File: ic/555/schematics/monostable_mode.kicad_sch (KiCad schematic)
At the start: 7 parts, among them U1 7555

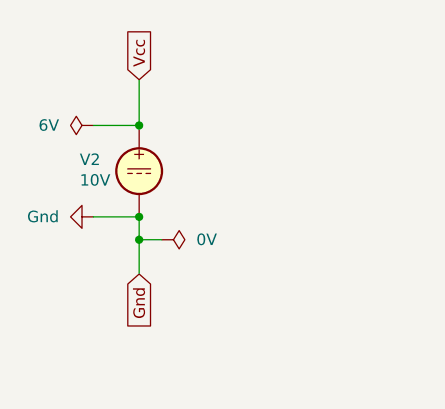
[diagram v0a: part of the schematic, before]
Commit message: feat: add monostable mode 555 timer circuit documentation and schematics
Adds practical example of 555 timer in monostable mode and updates the
README.

Breaking changes: None

Resolves: None
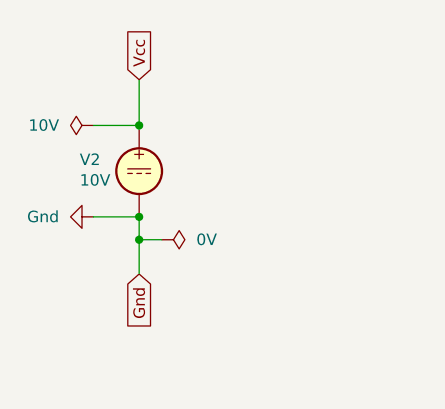
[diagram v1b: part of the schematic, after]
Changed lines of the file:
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@@
 			)
 		)
-		(property "Value" "6V"
+		(property "Value" "10V"
 			(at 21.59 26.6699 90)
 			(effects

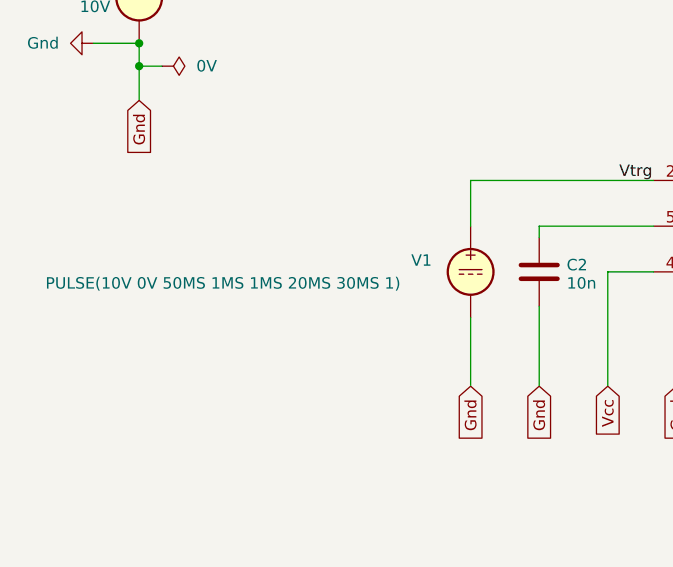
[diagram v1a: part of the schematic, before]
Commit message: feat: add LM741 op-amp with differential amplifier example
Adds the LM741 operational amplifier to the repository, including a
detailed schematic of an non inverting differential amplifier circuit.
The schematic is provided in KiCad format along with an SVG
version for easy viewing. Additionally, oscilloscope screenshots
demonstrate the amplifier's performance under various input conditions.

Breaking changes: None

Resolves: None
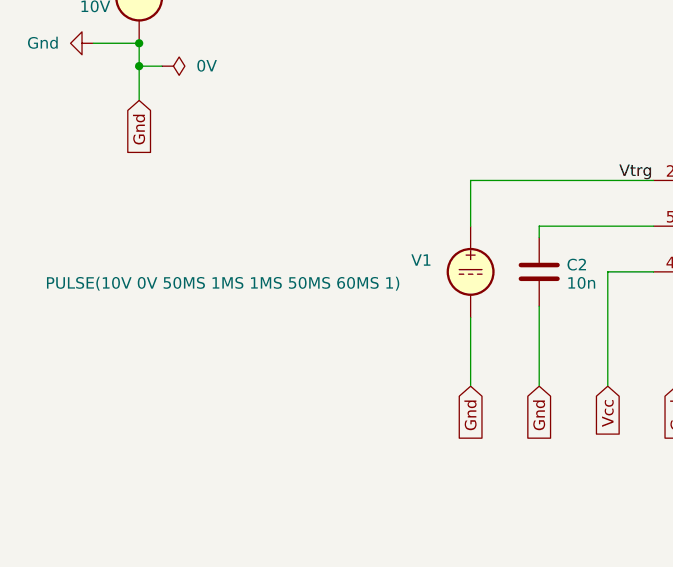
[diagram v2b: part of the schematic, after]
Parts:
- V1: value PULSE(10V 0V 50MS 1MS 1MS 20MS 30MS 1) -> PULSE(10V 0V 50MS 1MS 1MS 50MS 60MS 1)
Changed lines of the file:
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@@
 			)
 		)
-		(property "Value" "PULSE(10V 0V 50MS 1MS 1MS 20MS 30MS 1)"
+		(property "Value" "PULSE(10V 0V 50MS 1MS 1MS 50MS 60MS 1)"
 			(at 20.066 63.5 0)
 			(effects
